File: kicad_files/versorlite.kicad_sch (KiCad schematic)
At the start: 0 parts

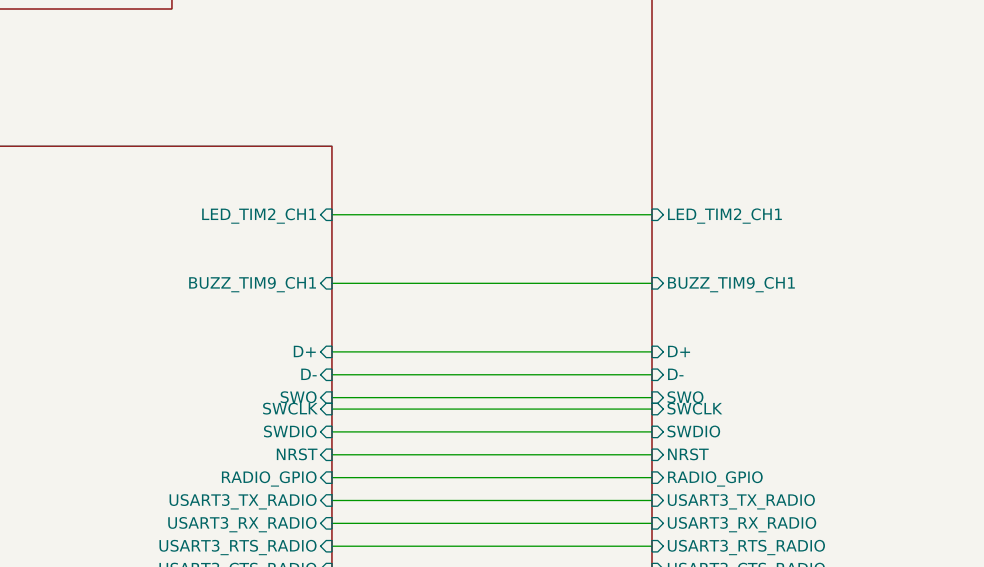
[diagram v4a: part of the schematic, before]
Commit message: fix buzzer
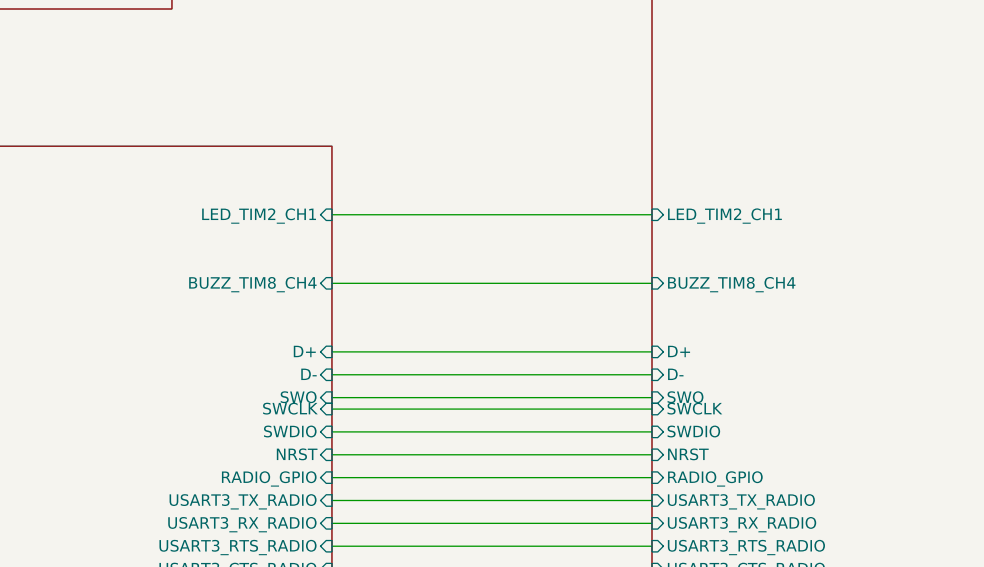
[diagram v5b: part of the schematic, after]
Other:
- sheet MCU ports: added BUZZ_TIM8_CH4; removed BUZZ_TIM9_CH1
- sheet Telemetry ports: added BUZZ_TIM8_CH4; removed BUZZ_TIM9_CH1
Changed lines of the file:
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@@
-			)
-		)
-		(pin "BUZZ_TIM9_CH1" input
-			(at 135.89 201.93 0)
-			(effects
-				(font
-					(size 1.27 1.27)
-				)
-				(justify right)
 			)
 		)
@@
 		(pin "USART3_TX_RADIO" input
 			(at 135.89 226.06 0)
+			(effects
+				(font
+					(size 1.27 1.27)
+				)
+				(justify right)
+			)
+		)
+		(pin "BUZZ_TIM8_CH4" input
+			(at 135.89 201.93 0)
 			(effects
 				(font
@@
 			)
 		)
-		(pin "BUZZ_TIM9_CH1" input
-			(at 171.45 201.93 180)
-			(effects
-				(font
-					(size 1.27 1.27)
-				)
-				(justify left)
-			)
-		)
 		(pin "BATT_READ" input
 			(at 274.32 203.2 0)
@@
 			)
 		)
+		(pin "BUZZ_TIM8_CH4" input
+			(at 171.45 201.93 180)
+			(effects
+				(font
+					(size 1.27 1.27)
+				)
+				(justify left)
+			)
+		)
